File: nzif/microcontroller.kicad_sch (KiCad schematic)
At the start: 25 parts, among them U1 MCP23017_SO

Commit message: cartoons on main2
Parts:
- gave numbers to parts that had none: 22
- renumbered C1 to C348, C2 to C350, U1 to U158
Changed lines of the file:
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@@
 		(dnp no)
 		(fields_autoplaced yes)
-		(property "Reference" "C?"
+		(property "Reference" "C345"
 			(at 118.11 33.0262 0)
 			(effects
@@
 		(dnp yes)
 		(fields_autoplaced yes)
-		(property "Reference" "R?"
+		(property "Reference" "R211"
 			(at 85.09 29.21 90)
 			(effects
@@
 		(dnp no)
 		(fields_autoplaced yes)
-		(property "Reference" "R?"
+		(property "Reference" "R213"
 			(at 193.04 63.5 90)
 			(effects
@@
 		(dnp no)
 		(fields_autoplaced yes)
-		(property "Reference" "#PWR?"
+		(property "Reference" "#PWR0385"
 			(at 189.23 45.72 0)
 			(effects
@@
 		(dnp no)
 		(fields_autoplaced yes)
-		(property "Reference" "C?"
+		(property "Reference" "C351"
 			(at 212.09 35.5662 0)
 			(effects
@@
 		(dnp no)
 		(fields_autoplaced yes)
-		(property "Reference" "#PWR?"
+		(property "Reference" "#PWR0393"
 			(at 226.06 152.4 0)
 			(effects
@@
 		(dnp no)
 		(fields_autoplaced yes)
-		(property "Reference" "#PWR?"
+		(property "Reference" "#PWR0391"
 			(at 209.55 45.72 0)
 			(effects
@@
 		(dnp no)
 		(fields_autoplaced yes)
-		(property "Reference" "C?"
+		(property "Reference" "C357"
 			(at 298.45 35.5662 0)
 			(effects
@@
 		(dnp no)
 		(fields_autoplaced yes)
-		(property "Reference" "#PWR01"
+		(property "Reference" "#PWR0387"
 			(at 195.58 189.23 0)
 			(effects
@@
 		(dnp no)
 		(fields_autoplaced yes)
-		(property "Reference" "#PWR?"
+		(property "Reference" "#PWR0395"
 			(at 255.27 45.72 0)
 			(effects
@@
 		(dnp no)
 		(fields_autoplaced yes)
-		(property "Reference" "C?"
+		(property "Reference" "C358"
 			(at 308.61 35.5662 0)
 			(effects
@@
 		(dnp no)
 		(fields_autoplaced yes)
-		(property "Reference" "C?"
+		(property "Reference" "C346"
 			(at 128.27 33.0262 0)
 			(effects
@@
 		(dnp no)
 		(fields_autoplaced yes)
-		(property "Reference" "R?"
+		(property "Reference" "R214"
 			(at 194.31 101.6 90)
 			(effects
@@
 		(dnp no)
 		(fields_autoplaced yes)
-		(property "Reference" "#PWR?"
+		(property "Reference" "#PWR0396"
 			(at 265.43 45.72 0)
 			(effects
@@
 		(dnp no)
 		(fields_autoplaced yes)
-		(property "Reference" "R?"
+		(property "Reference" "R210"
 			(at 73.66 40.64 90)
 			(effects
@@
 		(dnp no)
 		(fields_autoplaced yes)
-		(property "Reference" "#PWR?"
+		(property "Reference" "#PWR0392"
 			(at 215.9 251.46 0)
 			(effects
@@
 		(dnp no)
 		(fields_autoplaced yes)
-		(property "Reference" "C?"
+		(property "Reference" "C360"
 			(at 328.93 35.5662 0)
 			(effects
@@
 		(dnp no)
 		(fields_autoplaced yes)
-		(property "Reference" "C?"
+		(property "Reference" "C354"
 			(at 267.97 35.5662 0)
 			(effects
@@
 		(dnp no)
 		(fields_autoplaced yes)
-		(property "Reference" "R?"
+		(property "Reference" "R212"
 			(at 184.15 66.04 90)
 			(effects
@@
 		(dnp no)
 		(fields_autoplaced yes)
-		(property "Reference" "#PWR04"
+		(property "Reference" "#PWR?"
 			(at 160.02 170.18 0)
 			(effects
@@
 				)
 			)
+			(project "nzif"
+				(path "/fe42ca2f-2bb8-4d5a-9e84-807788ed632f/27cecad5-c0fc-4afc-95d0-cabdd6a56668"
+					(reference "#PWR?")
+					(unit 1)
+				)
+			)
 		)
 	)
@@
 		(dnp no)
 		(fields_autoplaced yes)
-		(property "Reference" "#PWR?"
+		(property "Reference" "#PWR0397"
 			(at 275.59 45.72 0)
 			(effects
@@
 		(dnp no)
 		(fields_autoplaced yes)
-		(property "Reference" "C?"
+		(property "Reference" "C356"
 			(at 288.29 35.5662 0)
 			(effects
@@
 		(dnp no)
 		(fields_autoplaced yes)
-		(property "Reference" "#PWR?"
+		(property "Reference" "#PWR0402"
 			(at 326.39 45.72 0)
 			(effects
@@
 		(dnp no)
 		(fields_autoplaced yes)
-		(property "Reference" "U?"
+		(property "Reference" "U157"
 			(at 121.92 53.3399 0)
 			(effects
@@
 		(dnp no)
 		(fields_autoplaced yes)
-		(property "Reference" "J?"
+		(property "Reference" "J112"
 			(at 43.18 46.9899 0)
 			(effects
@@
 		(dnp no)
 		(fields_autoplaced yes)
-		(property "Reference" "C2"
+		(property "Reference" "C350"
 			(at 208.28 179.0762 0)
 			(effects
@@
 		(dnp no)
 		(fields_autoplaced yes)
-		(property "Reference" "C?"
+		(property "Reference" "C353"
 			(at 257.81 35.5662 0)
 			(effects
@@
 		(dnp no)
 		(fields_autoplaced yes)
-		(property "Reference" "#PWR?"
+		(property "Reference" "#PWR0381"
 			(at 53.34 58.42 0)
 			(effects
@@
 		(dnp no)
 		(fields_autoplaced yes)
-		(property "Reference" "#PWR02"
+		(property "Reference" "#PWR0390"
 			(at 205.74 189.23 0)
 			(effects
@@
 		(dnp no)
 		(fields_autoplaced yes)
-		(property "Reference" "#PWR?"
+		(property "Reference" "#PWR0388"
 			(at 196.85 148.59 0)
 			(effects
@@
 		(dnp no)
 		(fields_autoplaced yes)
-		(property "Reference" "#PWR?"
+		(property "Reference" "#PWR0400"
 			(at 306.07 45.72 0)
 			(effects
@@
 		(dnp no)
 		(fields_autoplaced yes)
-		(property "Reference" "C?"
+		(property "Reference" "C349"
 			(at 201.93 35.5662 0)
 			(effects
@@
 		(dnp no)
 		(fields_autoplaced yes)
-		(property "Reference" "#PWR?"
+		(property "Reference" "#PWR0398"
 			(at 285.75 45.72 0)
 			(effects
@@
 		(dnp no)
 		(fields_autoplaced yes)
-		(property "Reference" "#PWR?"
+		(property "Reference" "#PWR0383"
 			(at 115.57 43.18 0)
 			(effects
@@
 		(dnp no)
 		(fields_autoplaced yes)
-		(property "Reference" "C?"
+		(property "Reference" "C347"
 			(at 191.77 35.5662 0)
 			(effects
@@
 		(dnp no)
 		(fields_autoplaced yes)
-		(property "Reference" "C?"
+		(property "Reference" "C352"
 			(at 247.65 35.5662 0)
 			(effects
@@
 		(dnp no)
 		(fields_autoplaced yes)
-		(property "Reference" "#PWR?"
+		(property "Reference" "#PWR0384"
 			(at 125.73 43.18 0)
 			(effects
@@
 		(dnp no)
 		(fields_autoplaced yes)
-		(property "Reference" "U1"
+		(property "Reference" "U158"
 			(at 218.0433 189.23 0)
 			(effects
@@
 		(dnp no)
 		(fields_autoplaced yes)
-		(property "Reference" "#PWR?"
+		(property "Reference" "#PWR0394"
 			(at 245.11 45.72 0)
 			(effects
@@
 		(dnp no)
 		(fields_autoplaced yes)
-		(property "Reference" "U?"
+		(property "Reference" "U159"
 			(at 228.2033 144.78 0)
 			(effects
@@
 		(dnp no)
 		(fields_autoplaced yes)
-		(property "Reference" "#PWR?"
+		(property "Reference" "#PWR0389"
 			(at 199.39 45.72 0)
 			(effects
@@
 		(dnp no)
 		(fields_autoplaced yes)
-		(property "Reference" "C?"
+		(property "Reference" "C359"
 			(at 318.77 35.5662 0)
 			(effects
@@
 		(dnp no)
 		(fields_autoplaced yes)
-		(property "Reference" "#PWR?"
+		(property "Reference" "#PWR0382"
 			(at 110.49 73.66 0)
 			(effects
@@
 		(dnp no)
 		(fields_autoplaced yes)
-		(property "Reference" "#PWR?"
+		(property "Reference" "#PWR0399"
 			(at 295.91 45.72 0)
 			(effects
@@
 		(dnp no)
 		(fields_autoplaced yes)
-		(property "Reference" "C?"
+		(property "Reference" "C355"
 			(at 278.13 35.5662 0)
 			(effects
@@
 		(dnp no)
 		(fields_autoplaced yes)
-		(property "Reference" "C1"
+		(property "Reference" "C348"
 			(at 198.12 179.0762 0)
 			(effects
@@
 		(dnp no)
 		(fields_autoplaced yes)
-		(property "Reference" "#PWR03"
+		(property "Reference" "#PWR0386"
 			(at 194.31 251.46 0)
 			(effects
@@
 		(dnp no)
 		(fields_autoplaced yes)
-		(property "Reference" "#PWR?"
+		(property "Reference" "#PWR0401"
 			(at 316.23 45.72 0)
 			(effects

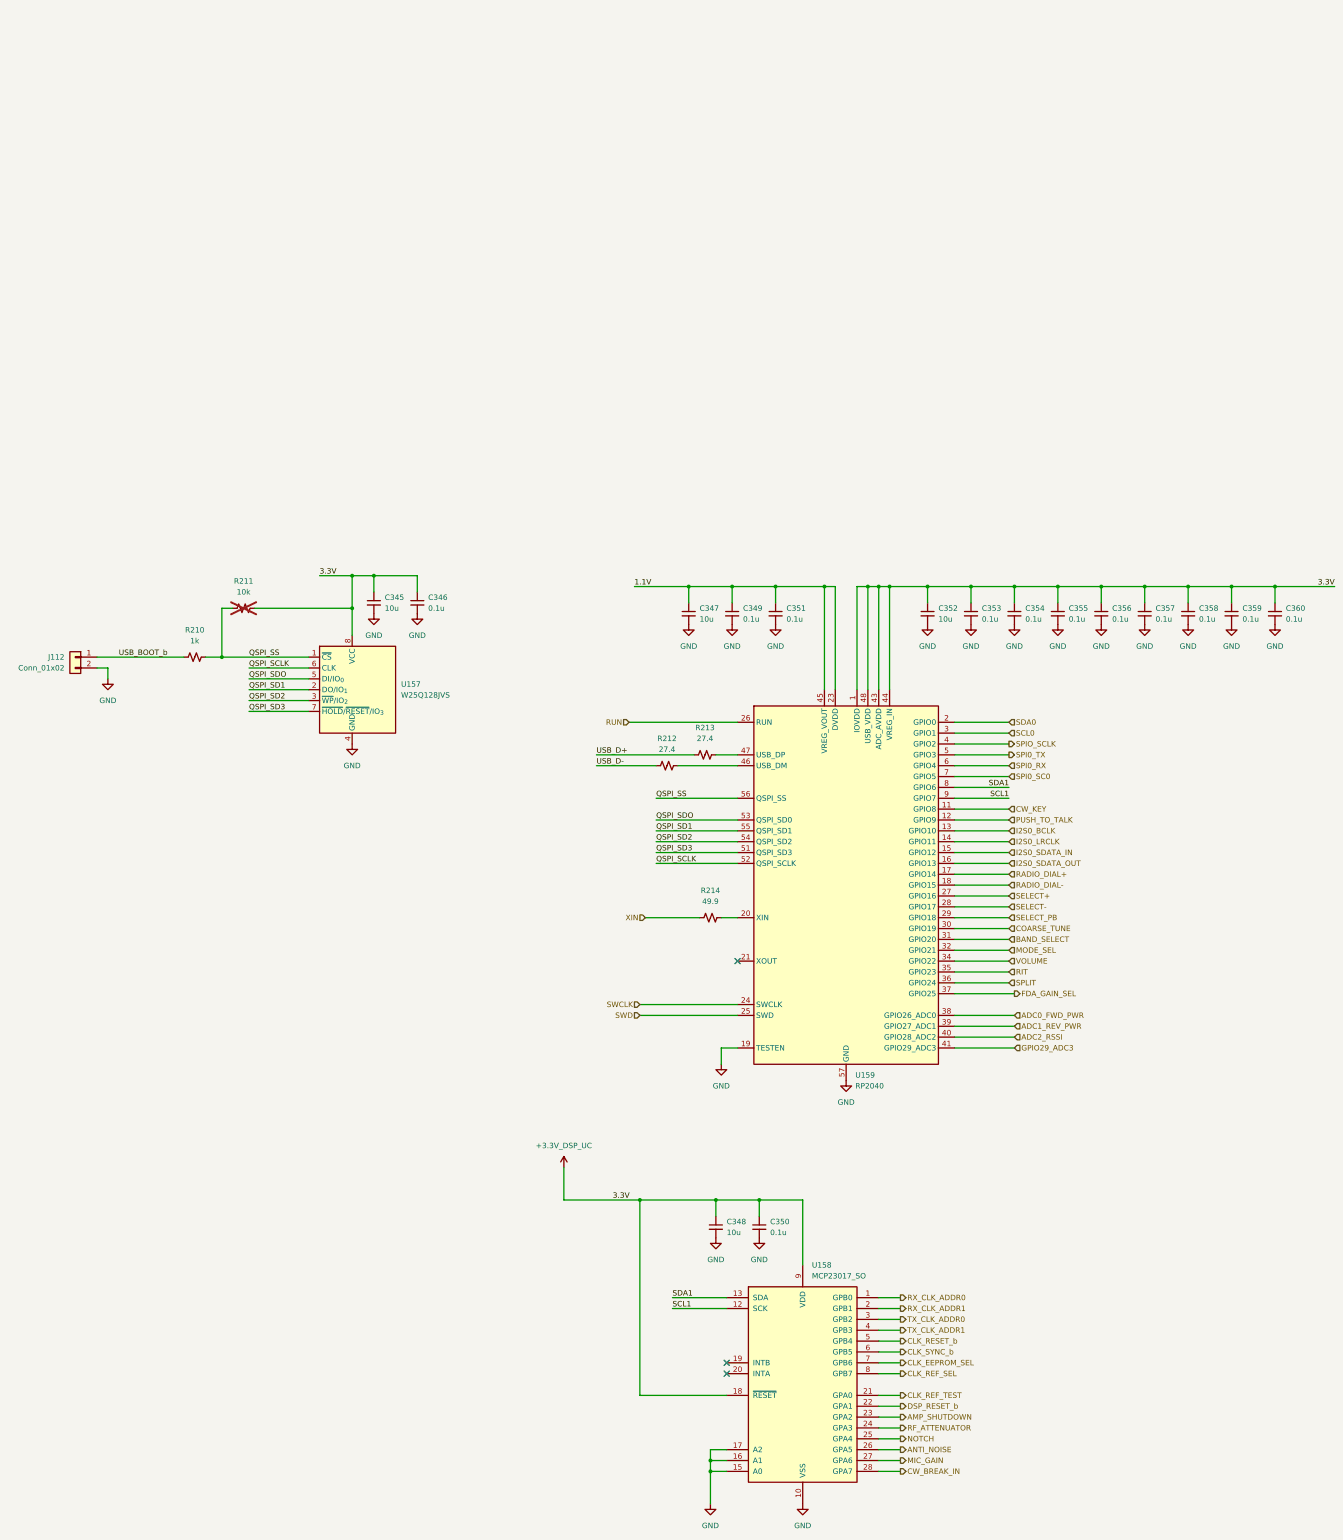
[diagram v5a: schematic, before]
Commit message: wire top sheet from rf front end through rx driver amps
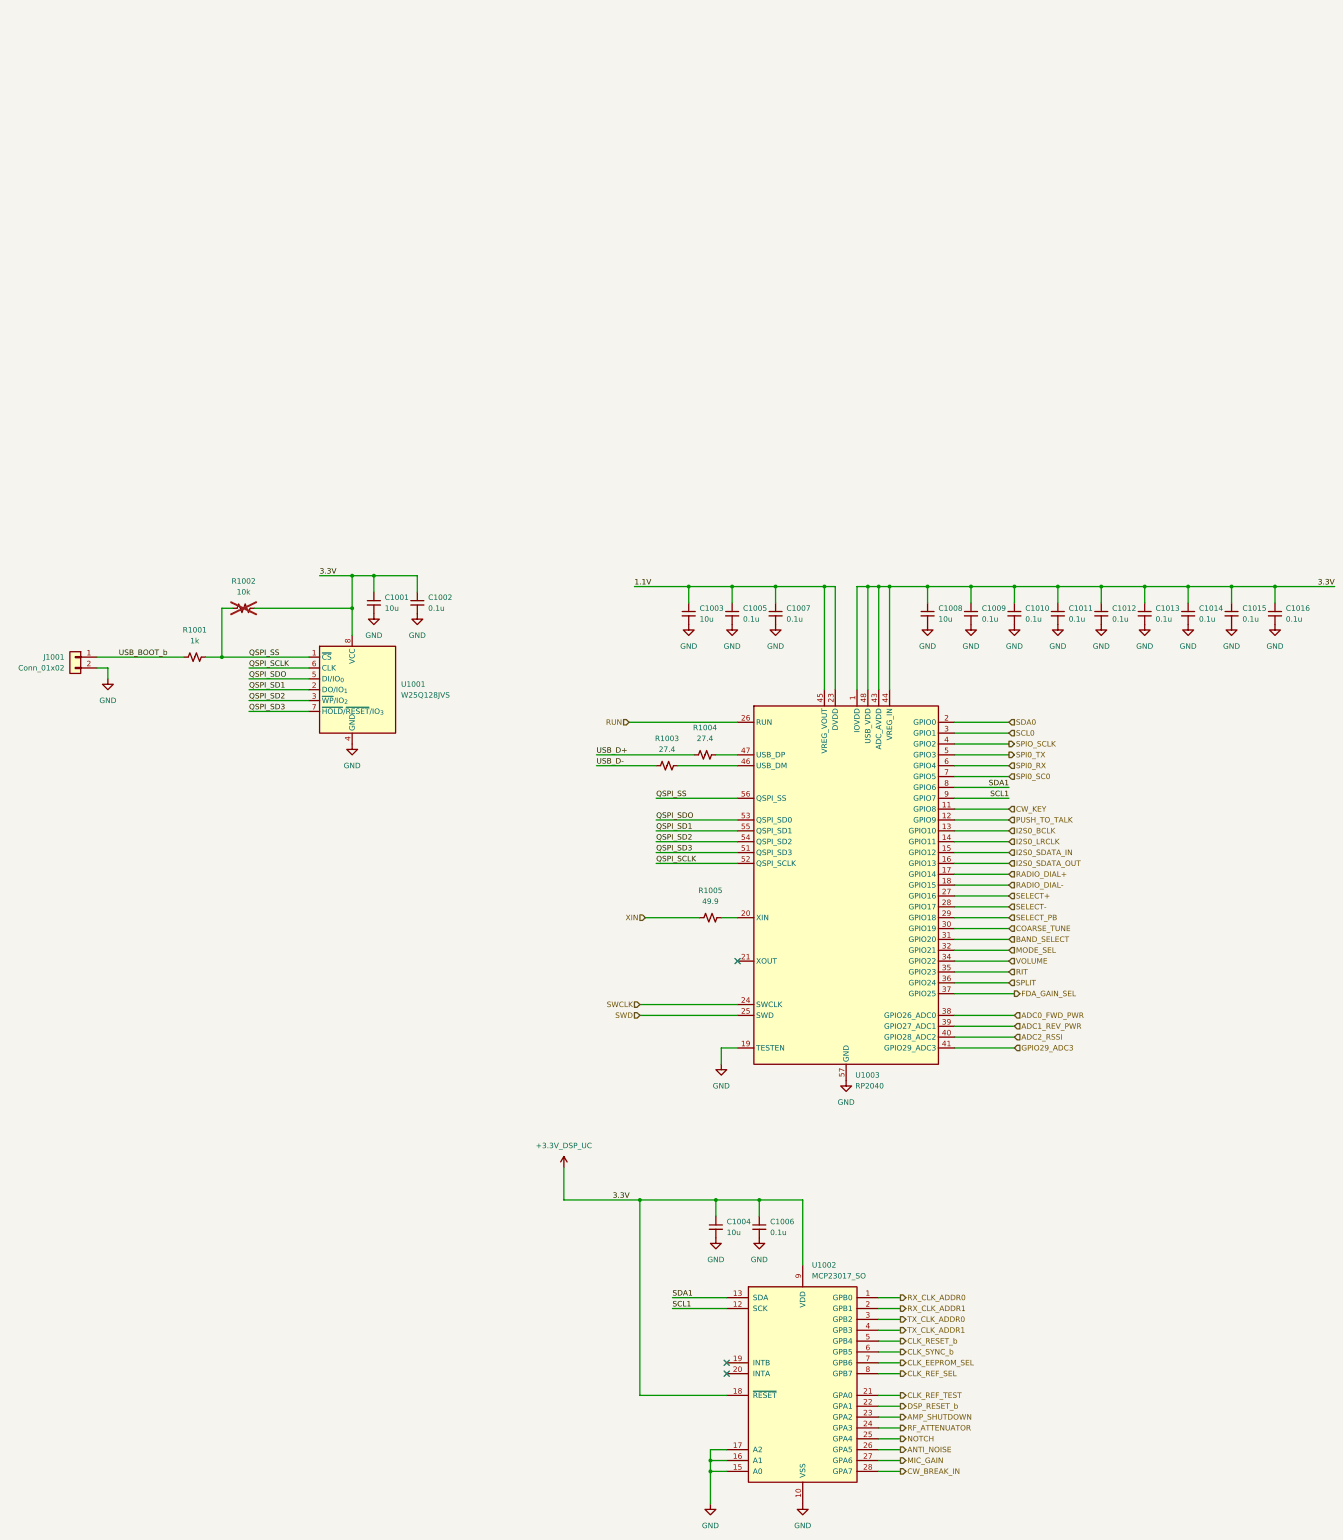
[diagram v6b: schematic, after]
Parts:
- renumbered C345 to C1001, C346 to C1002, C347 to C1003, C348 to C1004, C349 to C1005, C350 to C1006, C351 to C1007, C352 to C1008, C353 to C1009, C354 to C1010, C355 to C1011, C356 to C1012, C357 to C1013, C358 to C1014, C359 to C1015, C360 to C1016, J112 to J1001, R210 to R1001, R211 to R1002, R212 to R1003, R213 to R1004, R214 to R1005, U157 to U1001, U158 to U1002, U159 to U1003

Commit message: updates to top level
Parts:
- removed C1001, C1003: 10u, symbol Device:C_Small
- removed C1002, C1005, C1007, C1009, C1010, C1011, C1012, C1013, C1014, C1015: 0.1u, symbol Device:C_Small
- removed J1001: Conn_01x02, symbol Connector_Generic:Conn_01x02
- removed R1001: 1k, symbol Device:R_Small_US
- removed R1002: 10k, symbol Device:R_Small_US
- removed R1003, R1004: 27.4, symbol Device:R_Small_US
- removed R1005: 49.9, symbol Device:R_Small_US
- removed U1001: W25Q128JVS, Package_SO:SOIC-8_5.3x5.3mm_P1.27mm, symbol Memory_Flash:W25Q128JVS
- removed U1003: RP2040, Package_DFN_QFN:QFN-56-1EP_7x7mm_P0.4mm_EP3.2x3.2mm, symbol MCU_RaspberryPi:RP2040
- added A1201: RaspberryPi_Pico, Module:RaspberryPi_Pico_SMD, symbol MCU_Module:RaspberryPi_Pico_Extensive
- added R1212, R1213: 100k, symbol Device:R_Small_US
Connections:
- net +3.3V_DSP_UC: now also A1201.36 (3V3)
- net ADC0_FWD_PWR: now also A1201.31 (GPIO26_ADC0)
- net ADC1_REV_PWR: now also A1201.32 (GPIO27_ADC1)
- net ADC2_RSSI: now also A1201.34 (GPIO28_ADC2)
- net BAND_SELECT: now also A1201.26 (GPIO20)
- net COARSE_TUNE: now also A1201.25 (GPIO19)
- net CW_KEY: now also A1201.11 (GPIO8)
- net FDA_GAIN_SEL: now also A1201.14 (GPIO10)
- net GND: now also A1201.13 (GND), A1201.18 (GND), A1201.23 (GND), A1201.28 (GND), A1201.3 (GND), A1201.33 (AGND), A1201.38 (GND), A1201.8 (GND), A1201.D2 (GND), R1212.2
- net MODE_SEL: now also A1201.27 (GPIO21)
- net PUSH_TO_TALK: now also A1201.12 (GPIO9)
- net RADIO_DIAL+: now also A1201.17 (GPIO13)
- net RADIO_DIAL-: now also A1201.19 (GPIO14)
- net RIT: now also A1201.16 (GPIO12)
- net SCL0: now also A1201.2 (GPIO1)
- net SCL1: now also A1201.10 (GPIO7)
- net SDA0: now also A1201.1 (GPIO0)
- net SDA1: now also A1201.9 (GPIO6)
- net SELECT+: now also A1201.21 (GPIO16)
- net SELECT-: now also A1201.22 (GPIO17)
- net SELECT_PB: now also A1201.24 (GPIO18)
- net SPI0_RX: now also A1201.6 (GPIO4)
- net SPI0_SC0: now also A1201.7 (GPIO5)
- net SPI0_TX: now also A1201.5 (GPIO3)
- net SPIO_SCLK: now also A1201.4 (GPIO2)
- net SPLIT: now also A1201.15 (GPIO11)
- net VOLUME: now also A1201.29 (GPIO22)
- new net: A1201.20 (GPIO15), R1212.1, R1213.2
- new net: A1201.40 (VBUS), R1213.1
- no-connect marks 3 -> 15
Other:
- moved on the sheet: C1008, C1016
